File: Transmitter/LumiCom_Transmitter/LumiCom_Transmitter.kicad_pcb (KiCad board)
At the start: 4 copper layers, 50 x 42 mm, 38 parts, among them J1 V, J2 IN_B, J3 IN_A, J4 OUT_B, J5 OUT_A, U1 OPA2675

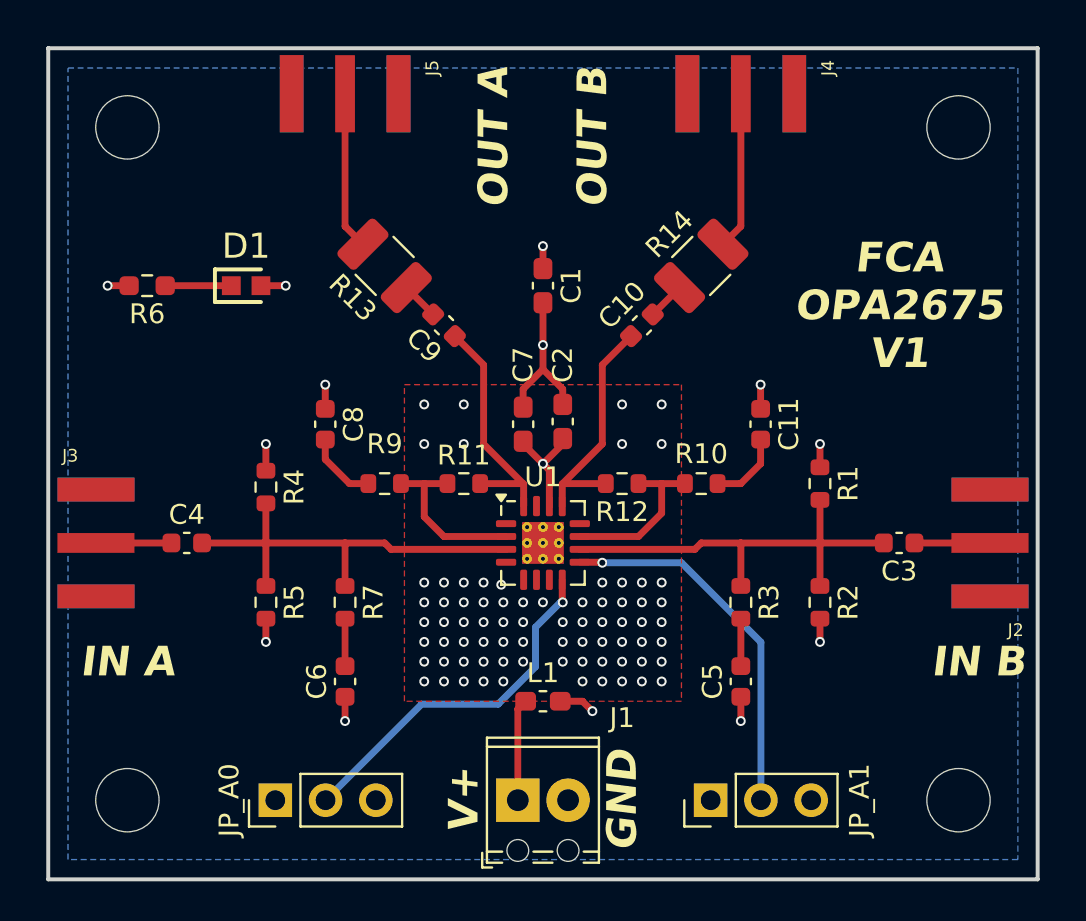
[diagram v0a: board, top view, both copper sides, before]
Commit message: Multiple updates
SMA, Screw terminals, track widths, added some optional 0 ohm bypass resistors
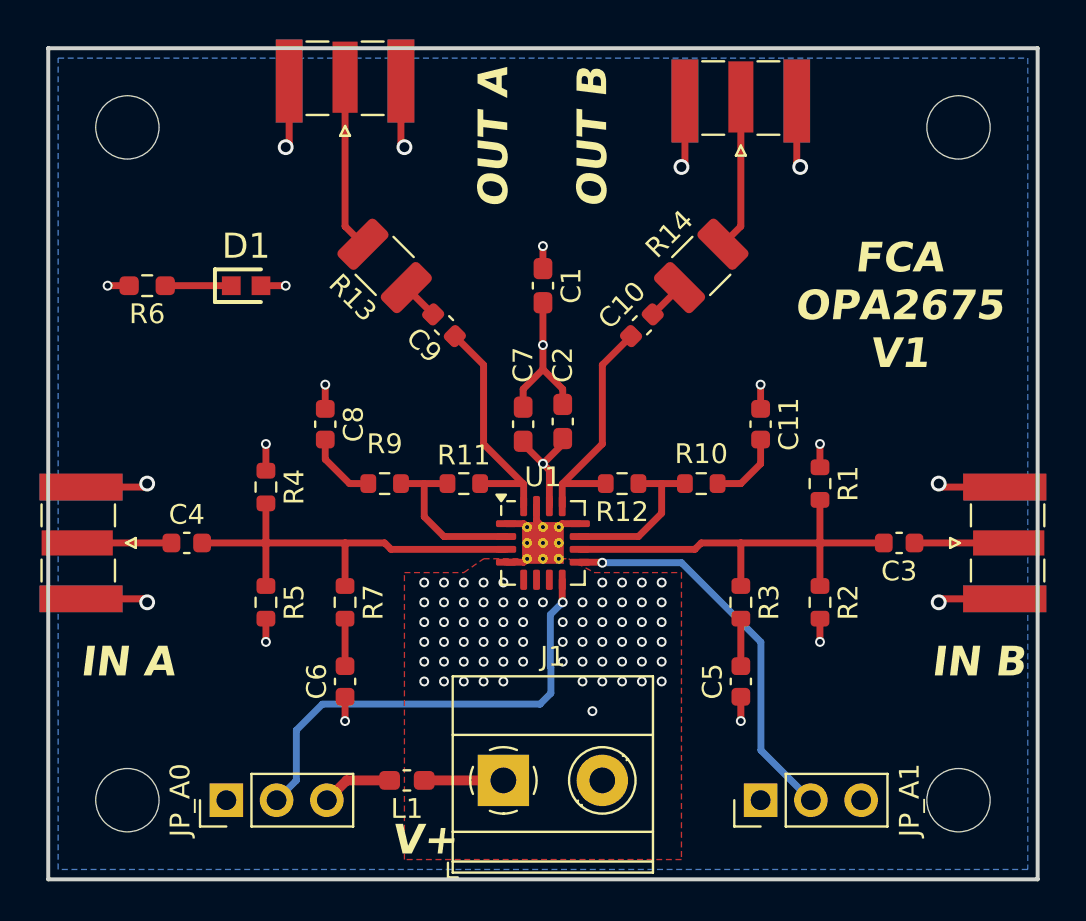
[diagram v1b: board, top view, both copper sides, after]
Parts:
- J1: footprint TerminalBlock_Phoenix:TerminalBlock_Phoenix_MPT-0,5-2-2.54_1x02_P2.54mm_Horizontal -> TerminalBlock_Phoenix:TerminalBlock_Phoenix_MKDS-1,5-2_1x02_P5.00mm_Horizontal
- J2, J3, J4, J5: footprint LumiCom_Transmitter:RFSOLUTIONS_CON-SMA-EDGE-S -> Connector_Coaxial:SMA_Samtec_SMA-J-P-X-ST-EM1_EdgeMount
- moved L1 7.95 mm to (118.1, 87.0), turned to 180 degrees
- moved JP_A1 2.53 mm to (136.0, 88.0)
- moved JP_A0 2.47 mm to (109.0, 88.0)
- moved J4 1.66 mm to (135.0, 52.7), turned to 180 degrees
- moved J1 1.24 mm to (123.0, 87.0)
- moved J5 0.66 mm to (115.0, 51.7), turned to 180 degrees
- moved J3 0.55 mm to (101.7, 75.0), turned to -90 degrees
- moved J2 0.55 mm to (148.3, 75.0), turned to 90 degrees
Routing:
- net GND: track 16.5 -> 48.4 mm
- net Net-(JP_A0-C): track 19.0 -> 23.6 mm
- net VCC: track 12.3 -> 14.0 mm
- net Net-(J1-Pin_1): track 5.16 -> 4.00 mm
- net Net-(JP_A1-C): track 18.8 -> 19.9 mm
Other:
- board text added: "Board Thicknees: 1.2mm 4 Layers"
- board text removed: "GND"
